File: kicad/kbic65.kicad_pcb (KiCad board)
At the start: 2 copper layers, 150 parts, among them U1 ProMicro

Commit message: More wiring
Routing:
- net ROW5: track 0.00 -> 308.0 mm
- net ROW3: track 0.00 -> 298.9 mm
- net ROW7: track 0.00 -> 287.1 mm
- net ROW0: track 0.00 -> 285.1 mm
- net ROW6: track 0.00 -> 284.2 mm
- net ROW1: track 0.00 -> 276.0 mm
- net ROW4: track 0.00 -> 271.1 mm
- net ROW2: track 0.00 -> 259.8 mm
- net ROW8: track 0.00 -> 252.0 mm
- net Net-(D_RWin1-Pad2): track 0.00 -> 118.2 mm
- net Net-(D_Dot1-Pad2): track 0.00 -> 101.9 mm
- net Net-(D_FwdSlsh1-Pad2): track 0.00 -> 88.5 mm
- net Net-(D_SemiCol1-Pad2): track 0.00 -> 73.2 mm
- net Net-(D_@1-Pad2): track 0.00 -> 68.0 mm
- net Net-(D_P1-Pad2): track 0.00 -> 65.2 mm
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
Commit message: Sooo much wiring
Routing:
- net Net-(D_LAlt1-Pad2): track 0.00 -> 123.0 mm
- net Net-(D_LWin1-Pad2): track 0.00 -> 115.6 mm
- net Net-(D_Space1-Pad2): track 0.00 -> 112.9 mm
- net Net-(D_RAlt1-Pad2): track 0.00 -> 111.6 mm
- net Net-(D_M1-Pad2): track 0.00 -> 102.6 mm
- net Net-(D_B1-Pad2): track 0.00 -> 97.7 mm
- net Net-(D_X1-Pad2): track 0.00 -> 97.1 mm
- net Net-(D_V1-Pad2): track 0.00 -> 94.0 mm
- net Net-(D_Z1-Pad2): track 0.00 -> 91.1 mm
- net Net-(D_C1-Pad2): track 0.00 -> 88.2 mm
- net Net-(D_Comma1-Pad2): track 0.00 -> 86.3 mm
- net Net-(D_N1-Pad2): track 0.00 -> 84.3 mm
- net Net-(D_D1-Pad2): track 0.00 -> 72.3 mm
- net Net-(D_S1-Pad2): track 0.00 -> 71.5 mm
- net Net-(D_G1-Pad2): track 0.00 -> 69.0 mm
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
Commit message: Wiring 4 life
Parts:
- moved D_LShift1 3.64 mm to (100.2, 53.2)
- moved D_LCtrl1 3.34 mm to (103.8, 53.2)
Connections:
- U1 pad 11: ROW1 -> ROW0
- U1 pad 12: ROW0 -> ROW1
- U1 pad 13: COL7 -> COL1
- U1 pad 14: COL6 -> COL0
- U1 pad 15: COL5 -> COL2
- U1 pad 16: COL4 -> COL3
- U1 pad 17: COL3 -> COL4
- U1 pad 18: COL2 -> COL5
- U1 pad 19: COL1 -> COL6
- U1 pad 20: COL0 -> COL7
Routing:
- net ROW5: track 308.0 -> 0.00 mm
- net ROW4: track 271.1 -> 0.00 mm
- net COL7: track 0.00 -> 270.8 mm
- net COL6: track 0.00 -> 239.9 mm
- net COL5: track 0.00 -> 210.1 mm
- net COL4: track 0.00 -> 176.1 mm
- net COL3: track 0.00 -> 142.6 mm
- net Net-(D_LCtrl1-Pad2): track 0.00 -> 116.7 mm
- net Net-(D_LShift1-Pad2): track 0.00 -> 101.6 mm
- net Net-(D_ISO_BKSLSH1-Pad2): track 0.00 -> 92.3 mm
- net Net-(D_Up1-Pad2): track 22.7 -> 113.8 mm
- net Net-(D_RCtrl1-Pad2): track 26.0 -> 110.5 mm
- net Net-(D_CpsLck1-Pad2): track 0.00 -> 82.8 mm
- net COL2: track 27.8 -> 109.2 mm
- net Net-(D_A1-Pad2): track 0.00 -> 79.4 mm
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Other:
- net class Robust added: clearance 0.5, trace_width 0.25, via_dia 0.8, via_drill 0.4

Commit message: Completed first version of full wiring
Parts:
- moved D_Q1 17.3 mm to (97.0, 53.2)
- moved D_LCtrl1 10.7 mm to (114.4, 53.2)
- moved D_LShift1 7.15 mm to (107.4, 53.2)
- moved D_A1 6.84 mm to (104.0, 53.2)
- moved D_CpsLck1 3.56 mm to (100.5, 53.2)
- moved D_ISO_BKSLSH1 3.44 mm to (110.8, 53.2)
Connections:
- U1 pad 10: ROW2 -> ROW3
- U1 pad 5: ROW7 -> ROW6
- U1 pad 6: ROW6 -> ROW7
- U1 pad 7: ROW5 -> ROW4
- U1 pad 8: ROW4 -> ROW5
- U1 pad 9: ROW3 -> ROW2
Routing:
- net ROW6: track 284.2 -> 118.8 mm
- net ROW5: track 0.00 -> 151.1 mm, vias 0 -> 1
- net ROW7: track 287.1 -> 157.5 mm, vias 0 -> 1
- net ROW4: track 0.00 -> 112.9 mm
- net ROW8: track 252.0 -> 356.6 mm
- net ROW3: track 259.3 -> 340.1 mm, vias 0 -> 1
- net ROW2: track 263.3 -> 312.0 mm
- net Net-(D_LCtrl1-Pad2): track 116.7 -> 147.9 mm
- net Net-(D_LShift1-Pad2): track 101.6 -> 128.1 mm
- net Net-(D_ISO_BKSLSH1-Pad2): track 92.3 -> 110.0 mm
- net Net-(D_CpsLck1-Pad2): track 82.8 -> 100.2 mm
- net Net-(D_Q1-Pad2): track 57.0 -> 44.5 mm
- net Net-(D_A1-Pad2): track 79.4 -> 72.8 mm
- net Net-(D_Tab1-Pad2): track 59.6 -> 65.1 mm
- net Net-(D_Esc1-Pad2): track 47.0 -> 42.5 mm
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
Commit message: Cleared wiring, starting over with default tracks
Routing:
- net ROW8: track 356.6 -> 0.00 mm
- net ROW3: track 340.1 -> 0.00 mm, vias 1 -> 0
- net ROW2: track 312.0 -> 0.00 mm
- net ROW0: track 300.5 -> 0.00 mm
- net ROW1: track 294.5 -> 0.00 mm
- net ROW7: track 157.5 -> 0.00 mm, vias 1 -> 0
- net ROW5: track 151.1 -> 0.00 mm, vias 1 -> 0
- net Net-(D_LCtrl1-Pad2): track 147.9 -> 0.00 mm
- net Net-(D_Left1-Pad2): track 137.7 -> 0.00 mm
- net Net-(D_LShift1-Pad2): track 128.1 -> 0.00 mm
- net Net-(D_LAlt1-Pad2): track 124.3 -> 0.00 mm
- net Net-(D_Down1-Pad2): track 121.1 -> 0.00 mm
- net ROW6: track 118.8 -> 0.00 mm
- net Net-(D_RWin1-Pad2): track 118.3 -> 0.00 mm
- net Net-(D_LWin1-Pad2): track 116.1 -> 0.00 mm
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
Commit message: Starting new wiring
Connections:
- U1 pad 10: ROW3 -> ROW4
- U1 pad 11: ROW0 -> ROW2
- U1 pad 12: ROW1 -> ROW0
- U1 pad 5: ROW6 -> ROW1
- U1 pad 6: ROW7 -> ROW3
- U1 pad 7: ROW4 -> ROW5
- U1 pad 8: ROW5 -> ROW7
- U1 pad 9: ROW2 -> ROW6
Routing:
- net ROW5: track 0.00 -> 362.1 mm
- net ROW7: track 0.00 -> 356.4 mm
- net ROW4: track 0.00 -> 346.6 mm
- net ROW8: track 0.00 -> 345.5 mm
- net ROW6: track 0.00 -> 338.4 mm
- net ROW3: track 0.00 -> 337.3 mm
- net ROW0: track 0.00 -> 315.9 mm
- net ROW2: track 0.00 -> 311.3 mm
- net ROW1: track 0.00 -> 297.5 mm
- net Net-(D_Esc1-Pad2): track 0.00 -> 195.4 mm
- net Net-(D_Tab1-Pad2): track 0.00 -> 176.0 mm
- net Net-(D_CpsLck1-Pad2): track 0.00 -> 159.0 mm
- net Net-(D_LShift1-Pad2): track 0.00 -> 143.0 mm
- net Net-(D_LCtrl1-Pad2): track 0.00 -> 122.3 mm
- net Net-(D_LWin1-Pad2): track 0.00 -> 99.1 mm
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
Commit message: Updated wiring, added drill holes and cut outline
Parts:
- added REF**: MountingHole_5mm_Custom, KBIC-Parts:MountingHole_5mm_KB, F.Cu at (355.6, 67.5)
- added REF**: MountingHole_5mm_Custom, KBIC-Parts:MountingHole_5mm_KB, F.Cu at (254.0, 67.5)
- added REF**: MountingHole_5mm_Custom, KBIC-Parts:MountingHole_5mm_KB, F.Cu at (152.4, 67.5)
- added REF**: MountingHole_5mm_Custom, KBIC-Parts:MountingHole_5mm_KB, F.Cu at (50.8, 67.5)
- moved D_Esc1 24.7 mm to (111.2, 53.2)
- moved D_Tab1 14.3 mm to (107.8, 53.2)
- moved D_3 14.2 mm to (135.5, 53.2)
- moved D_S1 14.1 mm to (124.5, 53.2)
- moved D_5 14.0 mm to (166.5, 53.2)
- moved D_4 13.9 mm to (163.0, 53.2)
- moved D_F1 13.9 mm to (156.0, 53.2)
- moved D_ISO_BKSLSH1 13.8 mm to (97.0, 53.2)
- moved D_2 13.7 mm to (131.5, 53.2)
- moved D_A1 10.5 mm to (93.5, 53.2)
- moved D_LAlt1 10.5 mm to (149.0, 53.2)
- moved D_C1 10.4 mm to (152.5, 53.2)
- moved D_Z1 10.4 mm to (121.2, 53.2)
- moved D_X1 10.3 mm to (145.5, 53.2)
- moved D_LWin1 10.2 mm to (118.0, 53.2)
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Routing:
- net Net-(D_Left1-Pad2): track 0.00 -> 147.8 mm
- net Net-(D_LAlt1-Pad2): track 0.00 -> 135.8 mm
- net Net-(D_Down1-Pad2): track 0.00 -> 128.1 mm
- net Net-(D_Right1-Pad2): track 0.00 -> 122.6 mm
- net Net-(D_Up1-Pad2): track 0.00 -> 119.7 mm
- net Net-(D_RCtrl1-Pad2): track 0.00 -> 117.6 mm
- net Net-(D_RWin1-Pad2): track 0.00 -> 117.0 mm
- net Net-(D_X1-Pad2): track 0.00 -> 113.1 mm
- net Net-(D_RAlt1-Pad2): track 0.00 -> 109.5 mm
- net Net-(D_Space1-Pad2): track 0.00 -> 108.3 mm
- net Net-(D_Dot1-Pad2): track 0.00 -> 106.3 mm
- net Net-(D_M1-Pad2): track 0.00 -> 104.3 mm
- net Net-(D_C1-Pad2): track 0.00 -> 102.9 mm
- net Net-(D_S1-Pad2): track 0.00 -> 100.5 mm
- net Net-(D_PgDn1-Pad2): track 0.00 -> 100.2 mm
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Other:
- board outline added: 313.3 x 123.8 mm
- net class Robust: clearance 0.5 -> 0.25

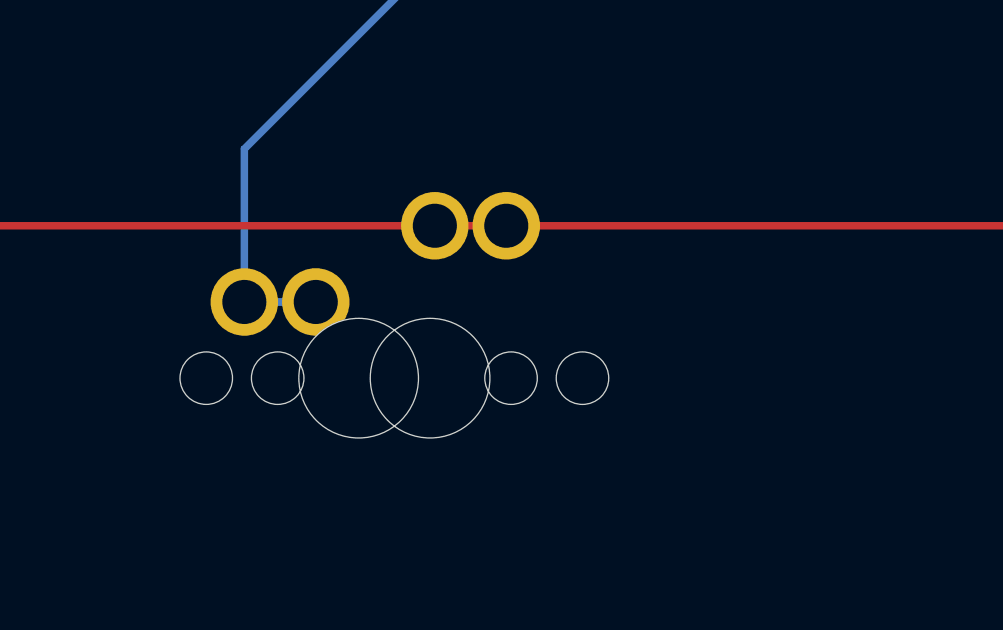
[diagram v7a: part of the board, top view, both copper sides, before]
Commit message: Fixed 6u spacebar
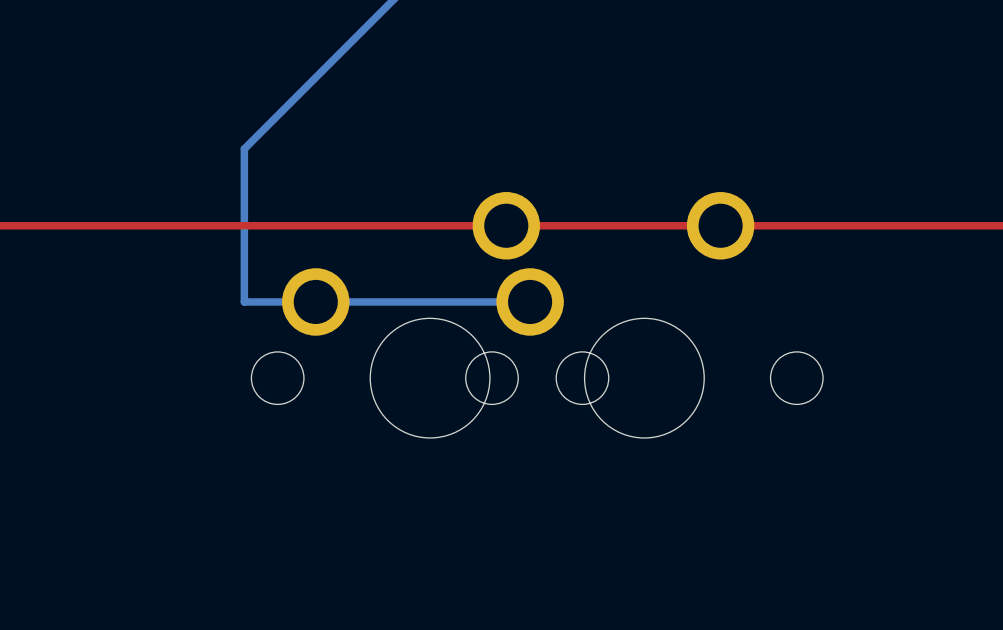
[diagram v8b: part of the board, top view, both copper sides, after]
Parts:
- MX_Space2_6u1: footprint MX_Only:MXOnly-6U-Centered-NoLED -> MX_Only:MXOnly-6U-NoLED
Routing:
- net Net-(D_Space1-Pad2): track 108.3 -> 115.4 mm
